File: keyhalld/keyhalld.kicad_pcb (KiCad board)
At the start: 4 copper layers, 261 x 71 mm, 103 parts, among them J1 Conn_01x06_Pin, J2 Conn_01x04_Pin, J3 USB_C_Receptacle_USB2.0_16P, SW1 RESET, SW10 HallSwitch, SW11 HallSwitch, SW12 HallSwitch, SW13 HallSwitch, SW14 HallSwitch, SW15 HallSwitch, SW16 HallSwitch, SW17 HallSwitch, SW18 HallSwitch, SW19 HallSwitch, SW2 USB_BOOT, SW20 HallSwitch, SW3 HallSwitch, SW4 HallSwitch, SW5 HallSwitch, SW6 HallSwitch, SW7 HallSwitch, SW8 HallSwitch, SW9 HallSwitch, U1 RP2350A, U10 DRV5055A4xDBZxQ1, U11 DRV5055A4xDBZxQ1, U12 DRV5055A4xDBZxQ1, U13 DRV5055A4xDBZxQ1, U14 DRV5055A4xDBZxQ1, U15 DRV5055A4xDBZxQ1, U16 DRV5055A4xDBZxQ1, U17 DRV5055A4xDBZxQ1, U18 DRV5055A4xDBZxQ1, U19 DRV5055A4xDBZxQ1, U2 CD74HC4067M, U20 DRV5055A4xDBZxQ1, U21 TLV1117-33, U22 USBLC6-2SC6, U23 TLV1117-33, U3 DRV5055A4xDBZxQ1, U4 DRV5055A4xDBZxQ1, U5 DRV5055A4xDBZxQ1, U6 DRV5055A4xDBZxQ1, U7 DRV5055A4xDBZxQ1, U8 DRV5055A4xDBZxQ1, U9 DRV5055A4xDBZxQ1, Y1 12MHz

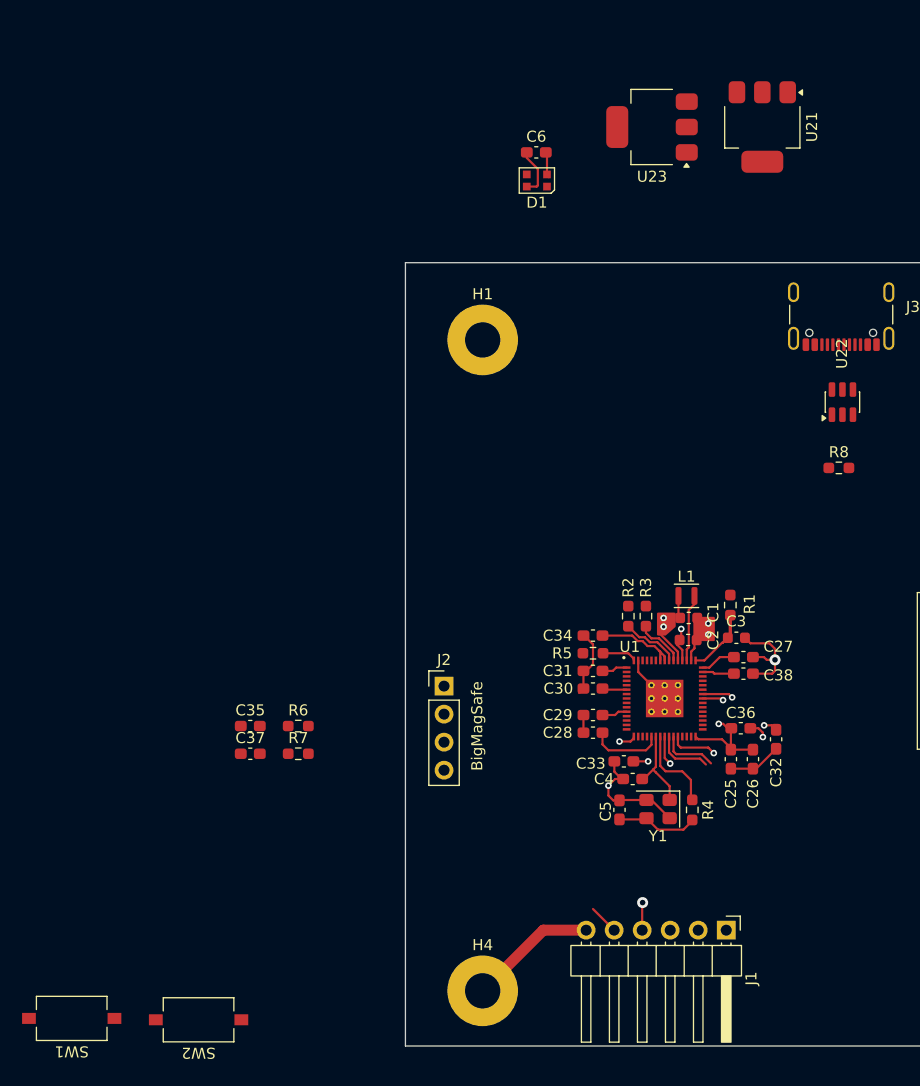
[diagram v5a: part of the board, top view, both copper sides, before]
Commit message: Sch refactor, power part done (for MCU)
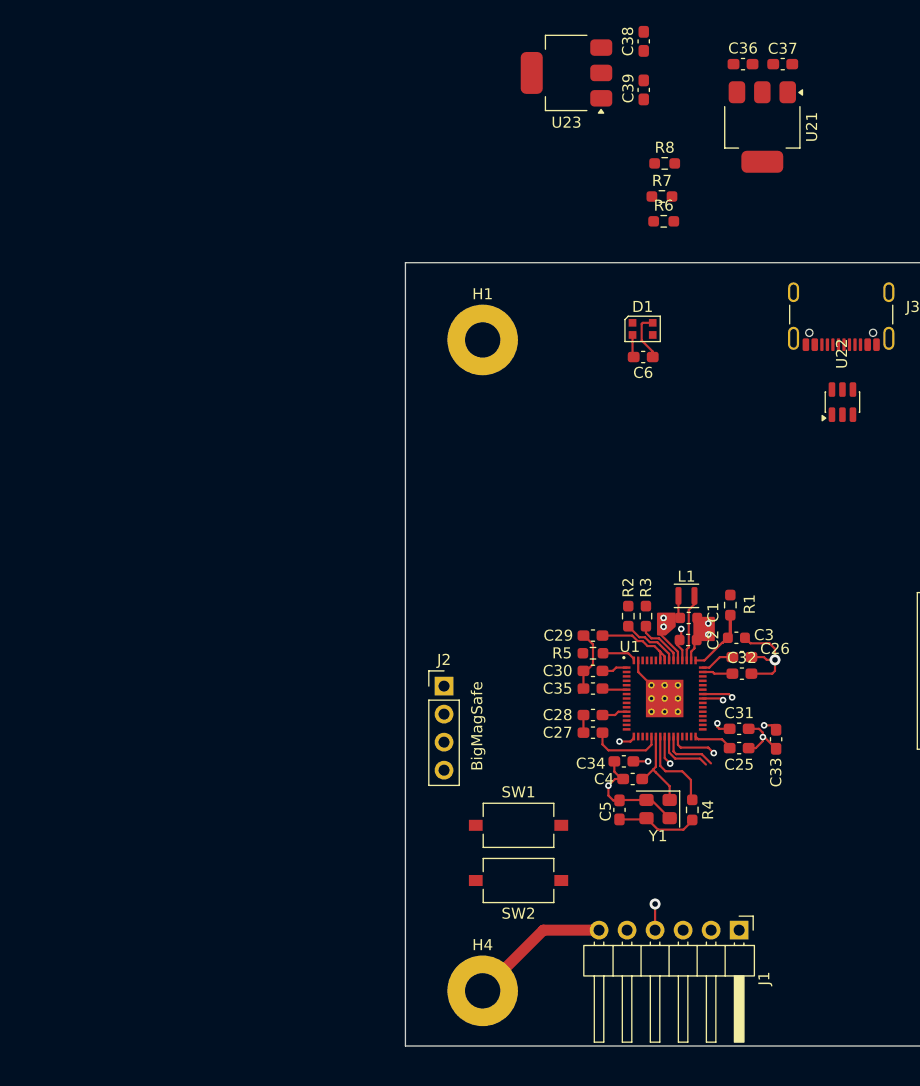
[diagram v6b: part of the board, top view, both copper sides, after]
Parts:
- removed the C26 at (175.5, 99.0)
- added C31: 100n, Capacitor_SMD:C_0603_1608Metric_Pad1.08x0.95mm_HandSolder, F.Cu at (174.2, 96.2)
- added C32: 100n, Capacitor_SMD:C_0603_1608Metric_Pad1.08x0.95mm_HandSolder, F.Cu at (174.5, 91.2)
- moved C36 74.8 mm to (174.6, 36.0)
- moved C38 73.8 mm to (165.6, 33.9), turned to 90 degrees
- moved C37 60.3 mm to (178.2, 36.0)
- moved R7 60.3 mm to (167.2, 48.0)
- moved R6 56.5 mm to (167.4, 50.2)
- moved C39 53.7 mm to (165.6, 38.3), turned to 90 degrees
- moved SW1 44.1 mm to (154.2, 105.0)
- moved R8 31.8 mm to (167.5, 45.0)
- moved SW2 31.6 mm to (154.2, 110.0)
- moved C6 20.9 mm to (165.6, 62.5), turned to 180 degrees
- moved D1 16.5 mm to (165.5, 60.0), turned to 0 degrees
- moved U23 9.17 mm to (158.6, 36.8)
- moved C29 4.80 mm to (161.0, 87.8)
- moved C35 4.80 mm to (161.0, 92.6)
- moved C25 1.25 mm to (174.2, 98.0), turned to 0 degrees
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- renumbered C27 to C26, C28 to C27, C29 to C28, C30 to C29, C31 to C30, C32 to C33, C33 to C34, C34 to C35, C35 to C36, C36 to C37, C37 to C38, C38 to C39
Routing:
- net +3.3V: track 38.5 -> 34.9 mm
- net DBG_TX: track 4.29 -> 1.57 mm

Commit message: Minor Zen preparations
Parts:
- moved C37 44.1 mm to (165.9, 78.3), turned to 180 degrees
- moved C38 43.1 mm to (184.8, 72.5)
- moved C39 42.7 mm to (184.8, 76.5)
- moved C36 42.6 mm to (169.5, 78.3), turned to 180 degrees
- moved U23 42.5 mm to (178.2, 74.5)
- moved U21 32.1 mm to (167.8, 72.6), turned to 90 degrees
- moved R6 14.0 mm to (158.4, 39.5)
- moved R7 10.3 mm to (158.2, 43.0)
- moved R8 9.03 mm to (158.5, 45.8), turned to 180 degrees
- moved C1 2.46 mm to (171.9, 87.2)
- moved C2 2.46 mm to (171.9, 89.2)
- moved C25 2.46 mm to (176.5, 99.0)
- moved C26 2.46 mm to (176.8, 90.8)
- moved C27 2.46 mm to (163.2, 97.6)
- moved C28 2.46 mm to (163.2, 96.0)
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
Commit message: route usb and ldo
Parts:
- moved R6 37.7 mm to (184.8, 66.5), turned to -90 degrees
- moved R7 33.9 mm to (182.8, 66.5), turned to 90 degrees
- moved R8 26.3 mm to (177.5, 64.0)
- moved C6 10.4 mm to (175.2, 58.9), turned to -90 degrees
- moved D1 7.28 mm to (172.7, 58.9), turned to 90 degrees
- moved U22 6.11 mm to (177.5, 66.5), turned to 180 degrees
- moved R3 5.21 mm to (163.2, 85.0), turned to 0 degrees
- moved R2 3.24 mm to (163.2, 86.5), turned to 180 degrees
- moved C36 1.53 mm to (171.0, 78.0), turned to 0 degrees
- moved C38 1.41 mm to (183.8, 71.5)
- moved C39 1.38 mm to (183.8, 75.5), turned to -90 degrees
- moved C37 0.90 mm to (166.8, 78.0)
- moved U21 0.10 mm to (167.8, 72.5)
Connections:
- net Net-(U1-USB_DM) renamed /USB_D-
- net Net-(U1-USB_DP) renamed /USB_D+
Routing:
- net +5V: track 4.46 -> 65.8 mm
- net WS2812_TX: track 0.00 -> 59.3 mm
- net D+: track 0.00 -> 34.9 mm
- net D-: track 0.00 -> 33.1 mm
- net +3.3V: track 34.9 -> 53.7 mm, vias 3 -> 5
- net /USB & Power/CONN_D+: track 0.00 -> 11.6 mm
- net /USB & Power/CONN_D-: track 0.00 -> 10.8 mm
- net /USB_D-: track 4.54 -> 9.18 mm
- net Net-(J3-CC2): track 0.00 -> 4.57 mm, vias 0 -> 2
- net Net-(J3-CC1): track 0.00 -> 4.16 mm
- net /USB_D+: track 5.33 -> 8.15 mm
- net +3.3VA: track 95.9 -> 98.3 mm
- net GND: track 107.6 -> 109.4 mm, vias 5 -> 6
